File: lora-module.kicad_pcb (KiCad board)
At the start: 4 copper layers, 20.3 x 22.5 mm, 53 parts, among them J101 Conn_Coaxial, J102 Conn_ARM_SWD_TagConnect_TC203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, Q101 PMN48XP, U201 STM32WLE5CCUx, U301 BALFHB-WL-05D3, U302 BGS12SN6E6327XTSA1, U401 SST26VF080A

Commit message: added bottom silkscreen
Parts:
- added G***: LOGO, bitmaps:kumquat_9.3x8, B.Cu at (137.0, 104.0)
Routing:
- net GND: vias 73 -> 74
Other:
- board text added: "1"
- board text added: "10"
- board text added: "10.23"
- board text added: "11"
- board text added: "2"
- board text added: "3"
- board text added: "4"
- board text added: "5"
- board text added: "6"
- board text added: "7"
- board text added: "8"
- board text added: "9"
- board text added: "B0"
- board text added: "BATT"
- board text added: "CLK"
- board text added: "DIO"
- board text added: "EXT"
- board text added: "GND"
- board text added: "LUMIA"
- board text added: "LoRa 865-923 module v0.1"
- board text added: "PWR"
- board text added: "RST"
- board text added: "SWO"
- board text added: "manakjiri.cz"

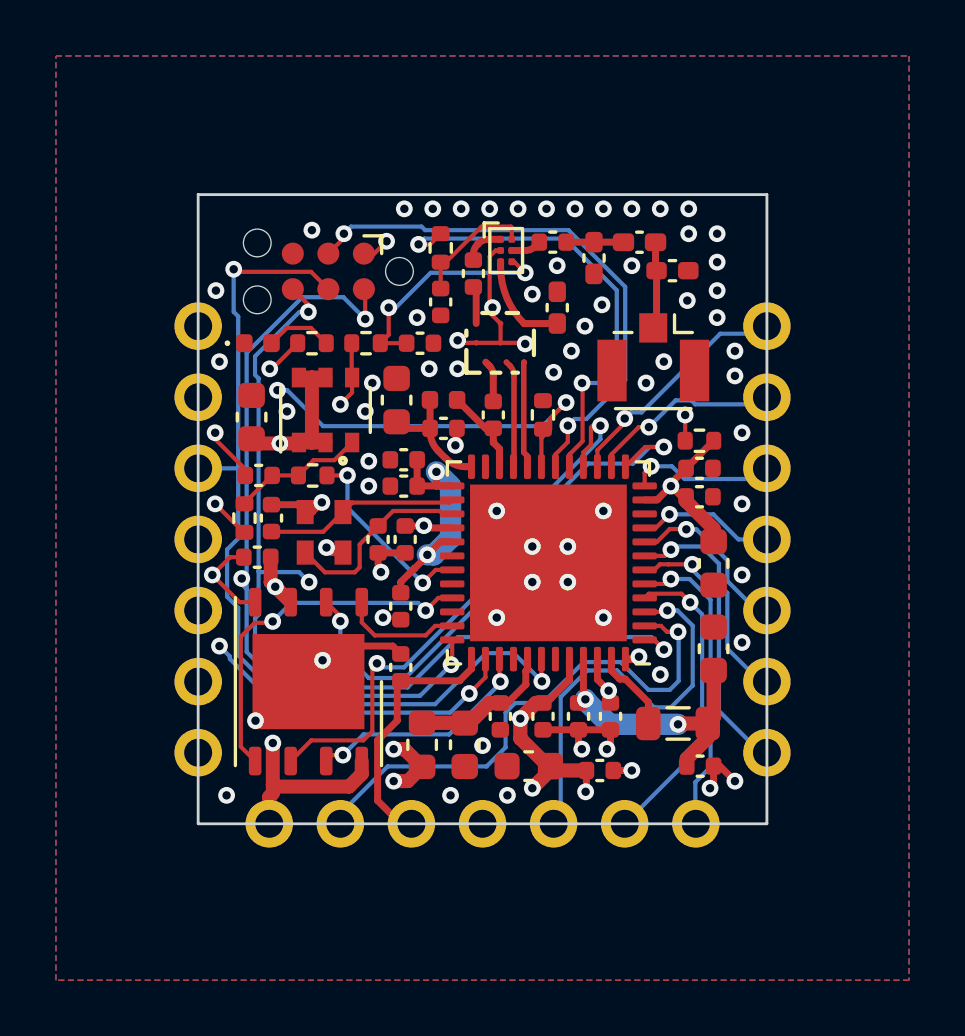
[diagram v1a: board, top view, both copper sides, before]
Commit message: groundplane settings tweak
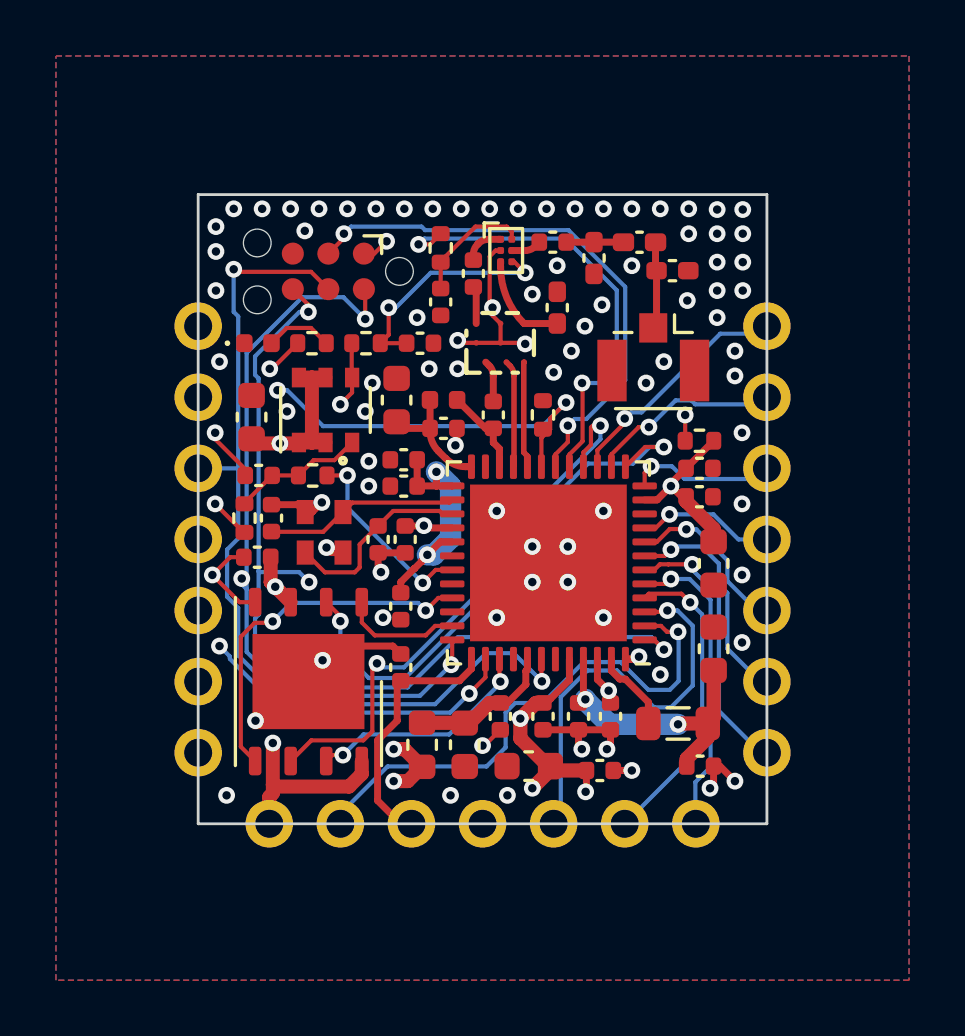
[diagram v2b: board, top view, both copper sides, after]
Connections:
- net /FLASH/MISO renamed /Memory/MISO
- net /FLASH/MOSI renamed /Memory/MOSI
- net /FLASH/SCK renamed /Memory/SCK
- net /FLASH/~{CS} renamed /Memory/~{CS}
- net /FLASH/~{HOLD} renamed /Memory/~{HOLD}
- net /STM32WL/~{VDD_SW_EN} renamed /~{VDD_SW_EN}
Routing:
- net GND: track 27.7 -> 28.5 mm, vias 74 -> 87

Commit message: batter layout of the SMPS section
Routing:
- net /STM32WL/VDDPA: track 27.6 -> 24.7 mm, vias 4 -> 5
- net /STM32WL/VLXSMPS: track 2.83 -> 1.90 mm
- net /IO9: track 11.0 -> 11.7 mm
- net /IO8: track 11.0 -> 11.5 mm
- added copper zone on F.Cu, net /STM32WL/VDDPA
- added copper zone on F.Cu, net /STM32WL/VLXSMPS

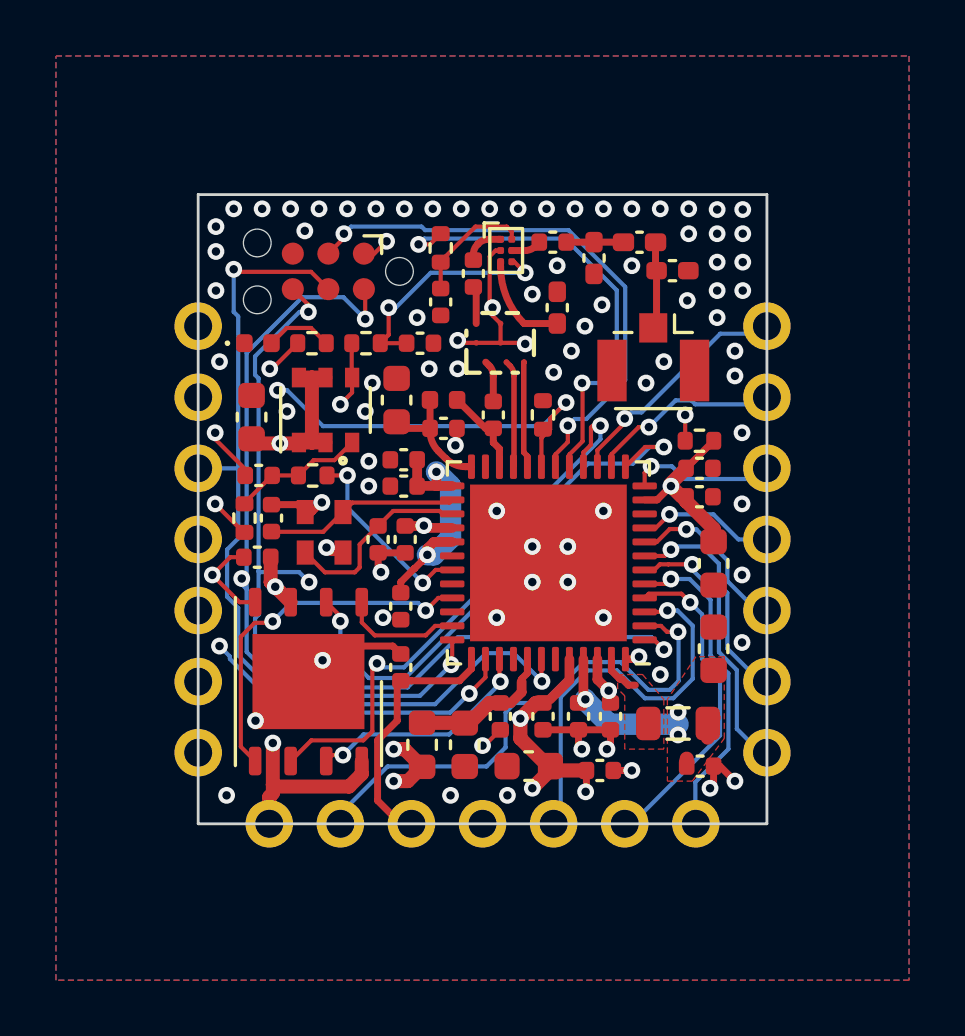
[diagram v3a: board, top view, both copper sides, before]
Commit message: bom tweaks
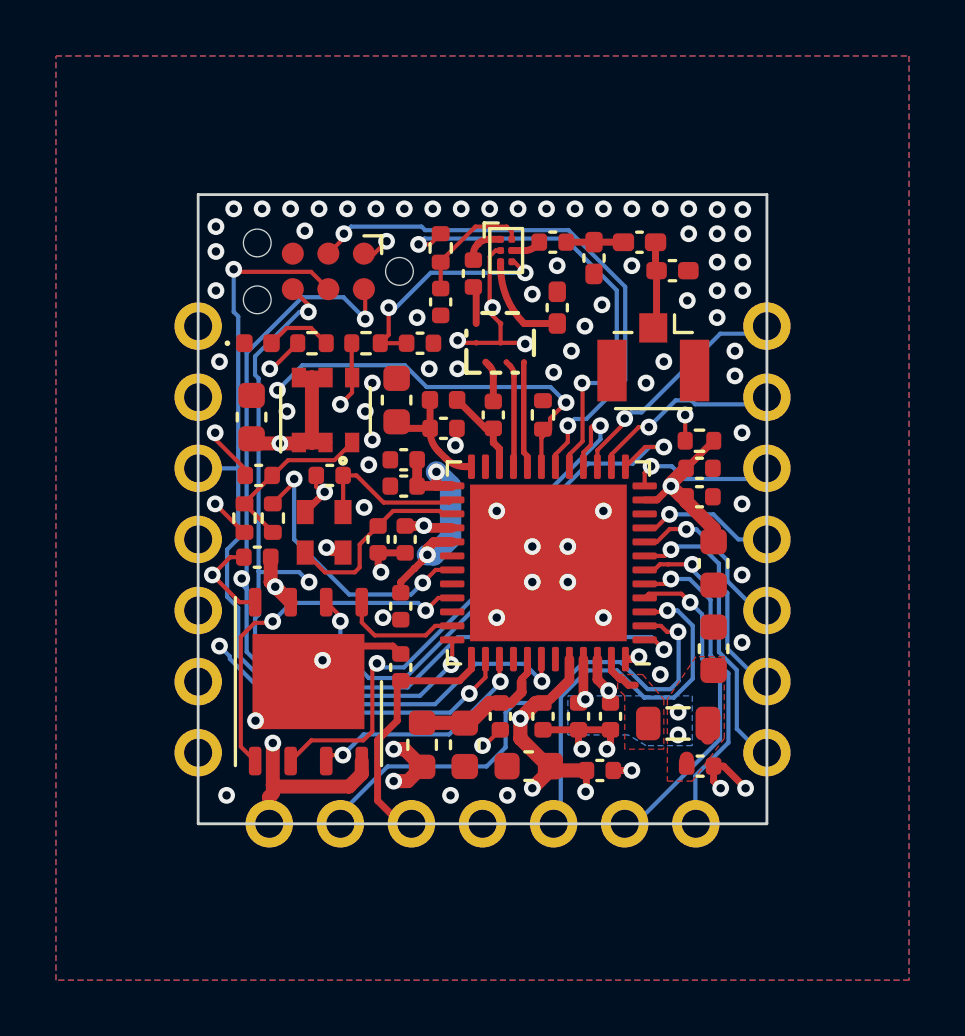
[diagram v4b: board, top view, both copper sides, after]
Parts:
- moved C202 2.58 mm to (129.2, 98.8), turned to 0 degrees
- moved R102 2.09 mm to (127.1, 100.3), turned to 90 degrees
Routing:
- net /STM32WL/VDDPA: track 24.7 -> 20.2 mm
- net /~{VDD_SW_EN}: track 6.93 -> 10.2 mm
- net Net-(Q101-G): track 4.77 -> 6.22 mm
- net Net-(U201-OSC_IN): track 6.93 -> 5.65 mm
- net GND: track 28.5 -> 28.8 mm, vias 87 -> 88
- added copper zone on B.Cu, net /STM32WL/VDDPA
